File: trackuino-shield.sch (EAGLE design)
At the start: 20 parts, among them IC2 AP1117, J5 J5MM, M2 HX1, Q1 IRLD110IRLD110, U1 LM60 int, X1 BU-SMA-V, X2 Vin, X3 LM60 ext, X4 Buzzer

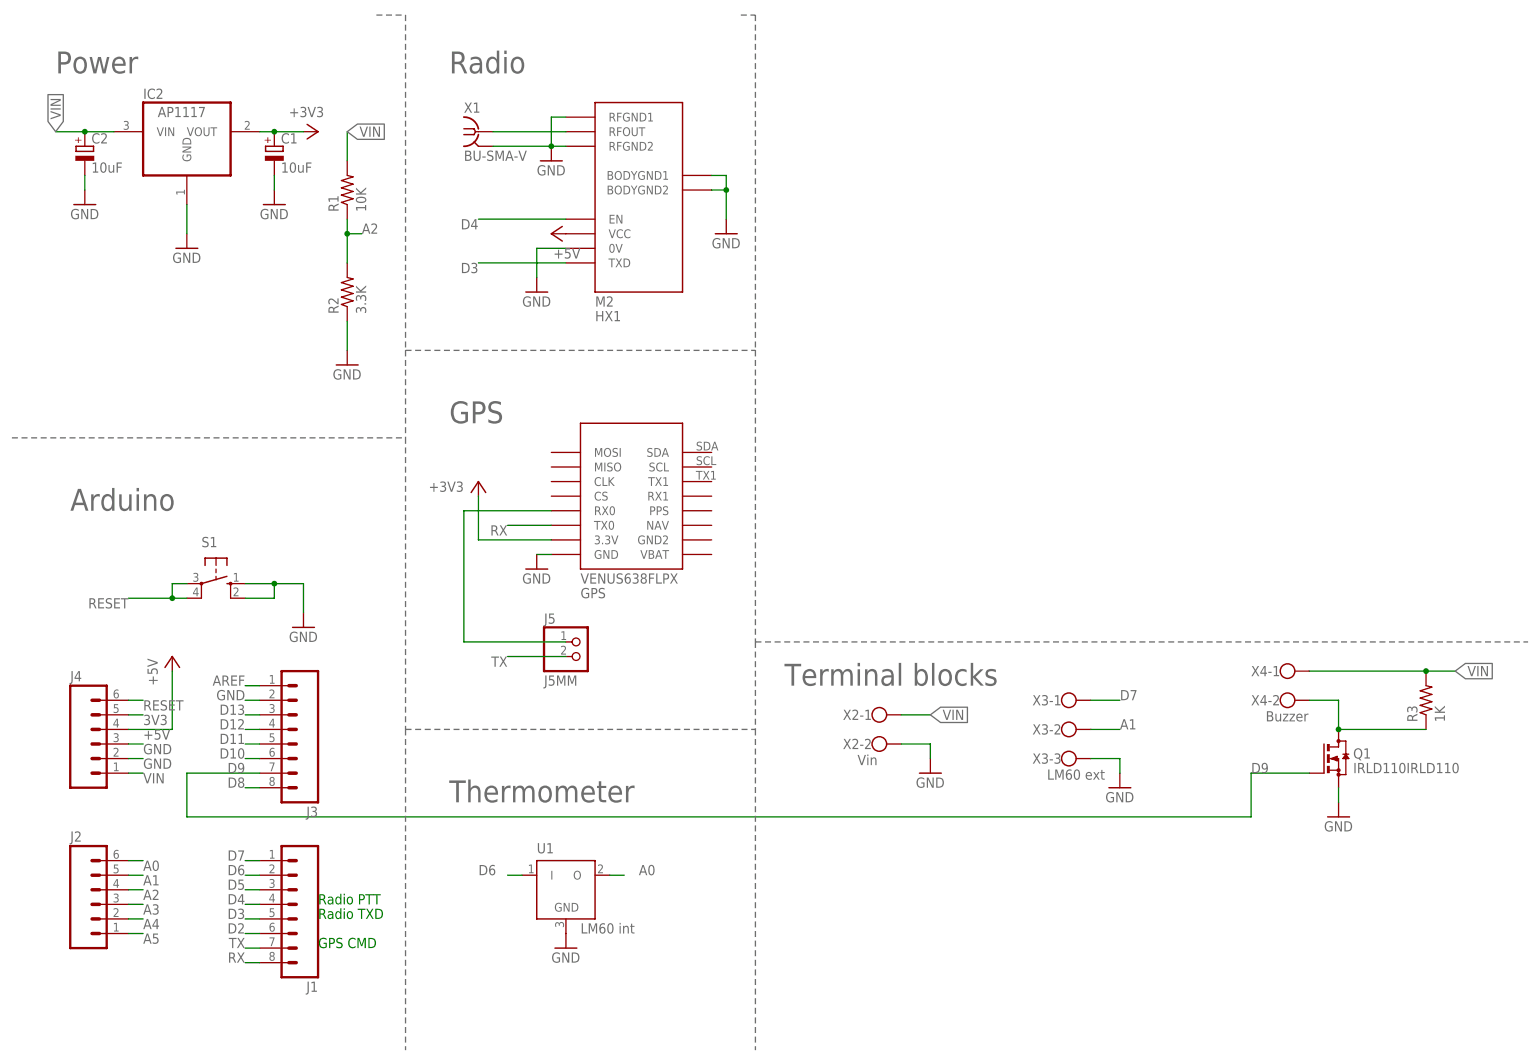
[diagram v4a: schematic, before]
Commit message: Reorg schematic and removed TX to GPS
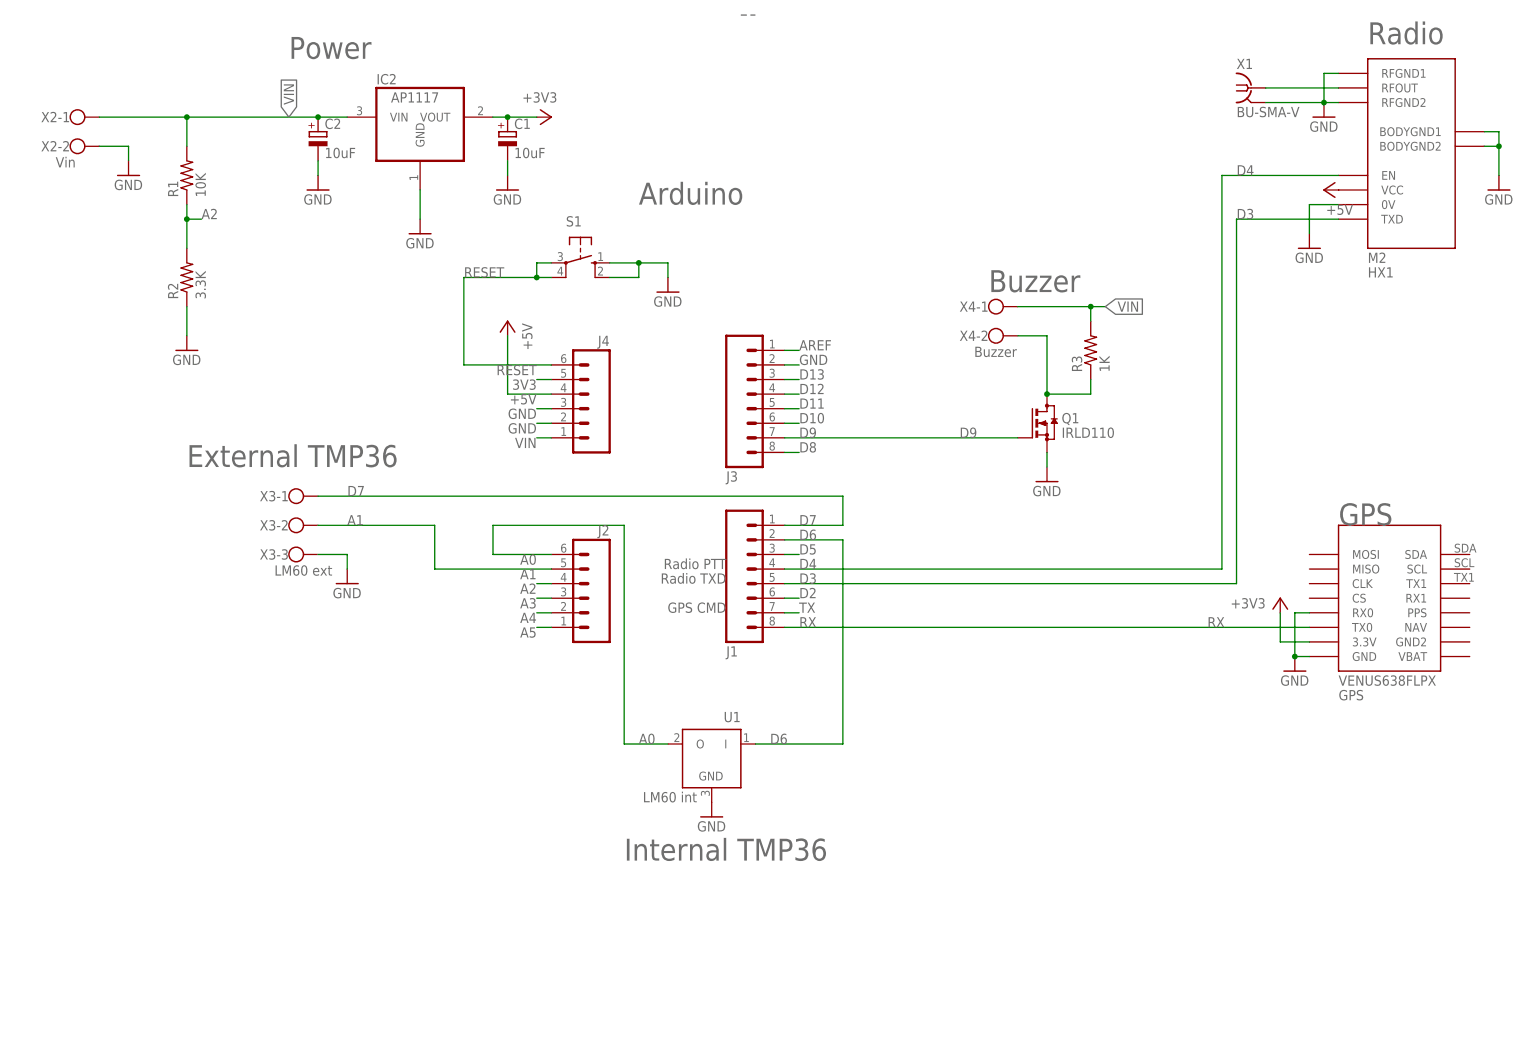
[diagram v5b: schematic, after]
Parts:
- removed J5: J5MM, pinhead:PINHD-1X2
- Q1: value IRLD110IRLD110 -> IRLD110; device First:IRLD110IRLD110 -> trackuino:IRLD110
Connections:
- removed net N$2: GPS.RX0, J5.1
- net GND: now also GPS.RX0
- net TX: no longer J5.2
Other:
- note added: "Buzzer"
- note added: "External TMP36"
- note added: "Internal TMP36"
- note removed: "Terminal blocks"
- note removed: "Thermometer"
- moved on the sheet: C1, C2, GPS, IC2, J1, J2, J3, J4, M2, Q1, R1, R2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

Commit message: Fixed sheaff's comments and separated the ground plane from the radiometrix
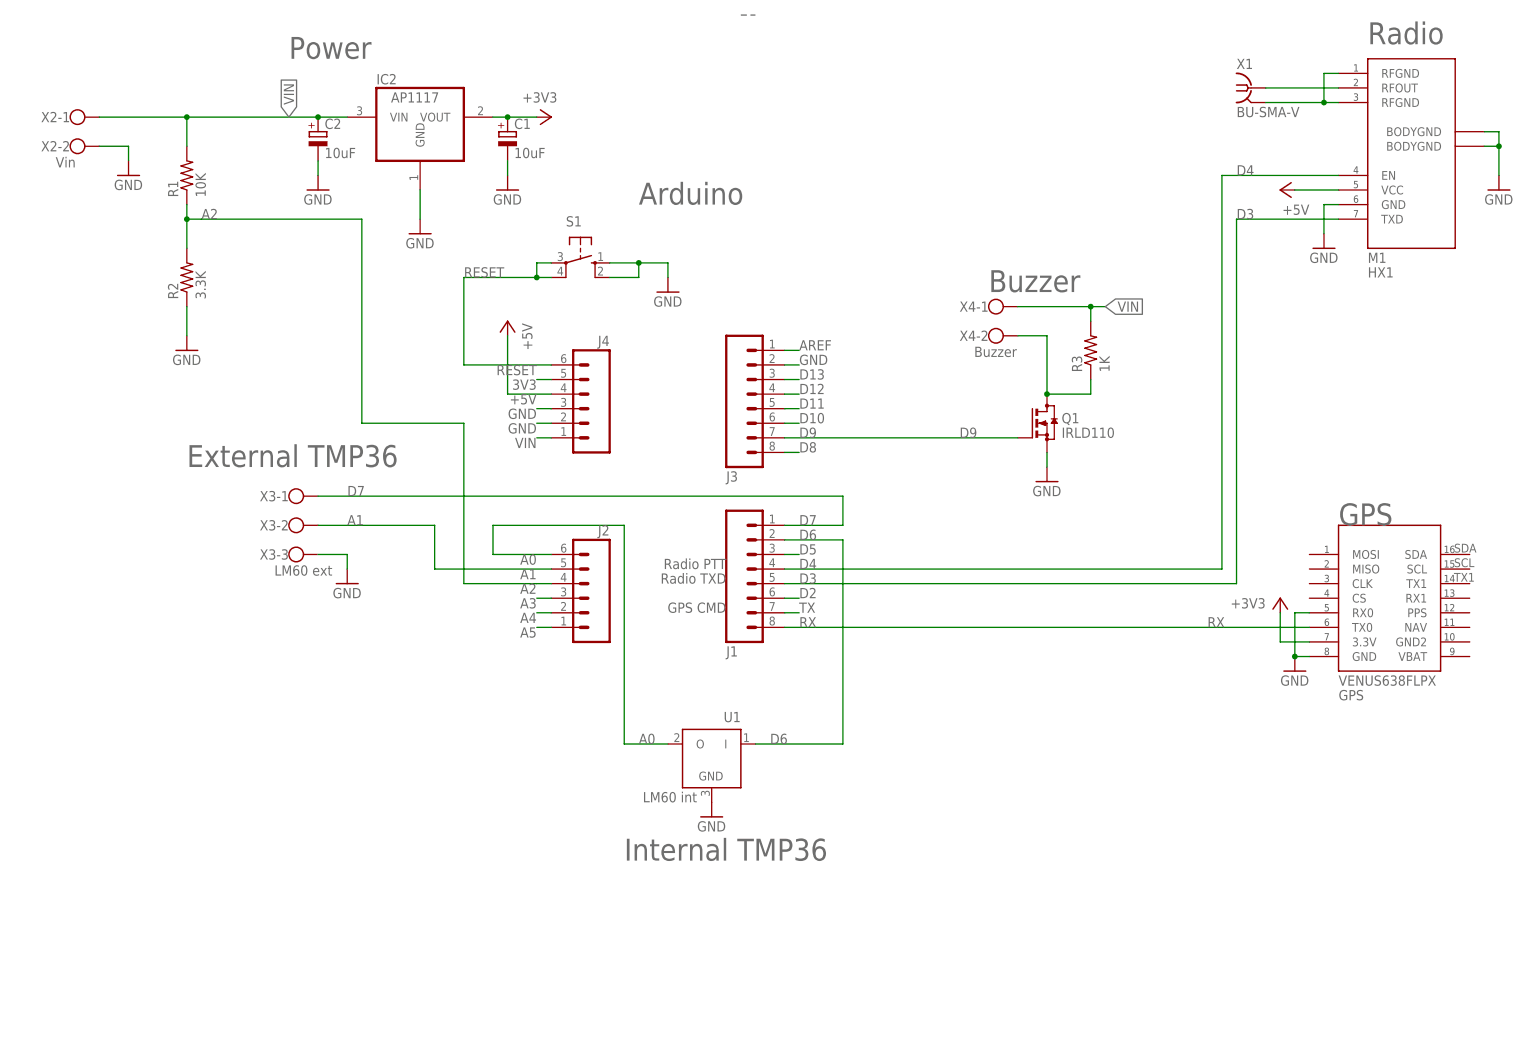
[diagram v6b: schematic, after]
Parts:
- J1, J3: device SparkFun:M08LOCK -> SparkFun-Connectors:M081X08
- J2, J4: device SparkFun:M06FEMALE_LOCK -> SparkFun-Connectors:M06SIP
- renumbered M2 to M1
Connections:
- removed net RFOUT: M1.RFOUT, X1G$1.1
- new net N$2: M1.RFOUT, X1.1
- new net RFGND: M1.RFGND@1, M1.RFGND@2, X1.2
- net GND: now also M1.BODYGND@1, M1.BODYGND@2, M1.GND; no longer M1.0V, M1.BODYGND1, M1.BODYGND2, M1.RFGND1, M1.RFGND2, X1G$1.GND

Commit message: Added logo
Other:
- moved on the sheet: J2
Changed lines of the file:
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@@
 <instance part="S1" gate="1" x="99.06" y="137.16" rot="R270"/>
 <instance part="J4" gate="G$1" x="99.06" y="111.76" rot="MR0"/>
-<instance part="J2" gate="G$1" x="99.06" y="78.74" rot="MR0"/>
+<instance part="J2" gate="G$1" x="99.06" y="76.2" rot="MR0"/>
 <instance part="J3" gate="G$1" x="129.54" y="114.3" rot="MR180"/>
 <instance part="J1" gate="G$1" x="129.54" y="83.82" rot="MR180"/>
@@
 <pinref part="U1" gate="G$1" pin="O"/>
 <wire x1="114.3" y1="53.34" x2="106.68" y2="53.34" width="0.1524" layer="91"/>
-<wire x1="93.98" y1="86.36" x2="83.82" y2="86.36" width="0.1524" layer="91"/>
-<label x="91.44" y="86.36" size="1.778" layer="95" rot="R180"/>
+<wire x1="93.98" y1="83.82" x2="83.82" y2="83.82" width="0.1524" layer="91"/>
+<label x="91.44" y="83.82" size="1.778" layer="95" rot="R180"/>
 <pinref part="J2" gate="G$1" pin="6"/>
-<wire x1="106.68" y1="53.34" x2="106.68" y2="91.44" width="0.1524" layer="91"/>
-<wire x1="106.68" y1="91.44" x2="83.82" y2="91.44" width="0.1524" layer="91"/>
-<wire x1="83.82" y1="91.44" x2="83.82" y2="86.36" width="0.1524" layer="91"/>
+<wire x1="106.68" y1="53.34" x2="106.68" y2="88.9" width="0.1524" layer="91"/>
+<wire x1="106.68" y1="88.9" x2="83.82" y2="88.9" width="0.1524" layer="91"/>
+<wire x1="83.82" y1="88.9" x2="83.82" y2="83.82" width="0.1524" layer="91"/>
 </segment>
 </net>
@@
 <wire x1="53.34" y1="91.44" x2="73.66" y2="91.44" width="0.1524" layer="91"/>
 <wire x1="73.66" y1="91.44" x2="73.66" y2="83.82" width="0.1524" layer="91"/>
-<label x="91.44" y="83.82" size="1.778" layer="95" rot="R180"/>
+<label x="91.44" y="81.28" size="1.778" layer="95" rot="R180"/>
 <pinref part="J2" gate="G$1" pin="5"/>
-<wire x1="73.66" y1="83.82" x2="93.98" y2="83.82" width="0.1524" layer="91"/>
+<wire x1="73.66" y1="83.82" x2="93.98" y2="81.28" width="0.1524" layer="91"/>
 </segment>
 </net>
@@
 <wire x1="30.48" y1="147.32" x2="30.48" y2="144.78" width="0.1524" layer="91"/>
 <wire x1="30.48" y1="144.78" x2="30.48" y2="139.7" width="0.1524" layer="91"/>
-<wire x1="30.48" y1="144.78" x2="33.02" y2="144.78" width="0.1524" layer="91"/>
 <junction x="30.48" y="144.78"/>
 <label x="33.02" y="144.78" size="1.778" layer="95"/>
 <pinref part="R1" gate="G$1" pin="1"/>
 <pinref part="R2" gate="G$1" pin="2"/>
-<wire x1="33.02" y1="144.78" x2="60.96" y2="144.78" width="0.2032" layer="91"/>
-<wire x1="60.96" y1="144.78" x2="60.96" y2="109.22" width="0.2032" layer="91"/>
-<wire x1="60.96" y1="109.22" x2="78.74" y2="109.22" width="0.2032" layer="91"/>
-<wire x1="78.74" y1="109.22" x2="78.74" y2="81.28" width="0.2032" layer="91"/>
-<wire x1="78.74" y1="81.28" x2="91.44" y2="81.28" width="0.2032" layer="91"/>
-<wire x1="93.98" y1="81.28" x2="91.44" y2="81.28" width="0.1524" layer="91"/>
-<label x="91.44" y="81.28" size="1.778" layer="95" rot="R180"/>
+<wire x1="30.48" y1="144.78" x2="17.78" y2="144.78" width="0.1524" layer="91"/>
+<wire x1="17.78" y1="144.78" x2="17.78" y2="78.74" width="0.1524" layer="91"/>
+<wire x1="17.78" y1="78.74" x2="93.98" y2="78.74" width="0.1524" layer="91"/>
+<label x="91.44" y="78.74" size="1.778" layer="95" rot="R180"/>
 <pinref part="J2" gate="G$1" pin="4"/>
 </segment>
 </net>
 <net name="A3" class="0">
-<segment>
-<wire x1="93.98" y1="78.74" x2="91.44" y2="78.74" width="0.1524" layer="91"/>
-<label x="91.44" y="78.74" size="1.778" layer="95" rot="R180"/>
-<pinref part="J2" gate="G$1" pin="3"/>
-</segment>
-</net>
-<net name="A4" class="0">
 <segment>
 <wire x1="93.98" y1="76.2" x2="91.44" y2="76.2" width="0.1524" layer="91"/>
 <label x="91.44" y="76.2" size="1.778" layer="95" rot="R180"/>
-<pinref part="J2" gate="G$1" pin="2"/>
-</segment>
-</net>
-<net name="A5" class="0">
+<pinref part="J2" gate="G$1" pin="3"/>
+</segment>
+</net>
+<net name="A4" class="0">
 <segment>
 <wire x1="93.98" y1="73.66" x2="91.44" y2="73.66" width="0.1524" layer="91"/>
 <label x="91.44" y="73.66" size="1.778" layer="95" rot="R180"/>
+<pinref part="J2" gate="G$1" pin="2"/>
+</segment>
+</net>
+<net name="A5" class="0">
+<segment>
+<wire x1="93.98" y1="71.12" x2="91.44" y2="71.12" width="0.1524" layer="91"/>
+<label x="91.44" y="71.12" size="1.778" layer="95" rot="R180"/>
 <pinref part="J2" gate="G$1" pin="1"/>
 </segment>
